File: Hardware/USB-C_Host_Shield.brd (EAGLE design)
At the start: 53.3 x 59.7 mm, 55 parts, among them J1 USB-C, J2 GPIN, J3 GPOUT, J4 Power Select, U1 ARDUINO_UNO_R3_SHIELDBASIC, U2 LM1117, U3 74HC4050, U5 MAX3421, U6 3.3V/150mA, Y1 12.0mhZ

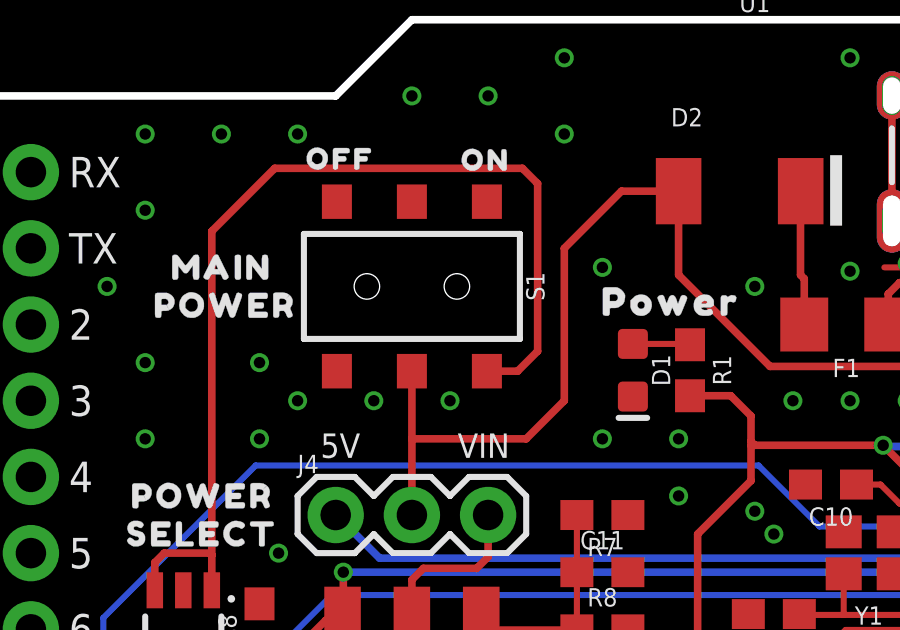
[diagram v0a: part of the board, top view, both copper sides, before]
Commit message: Added more GND vias and adjusted traces
Continued adding GNDing vias with adjusted traces for more polygon connection
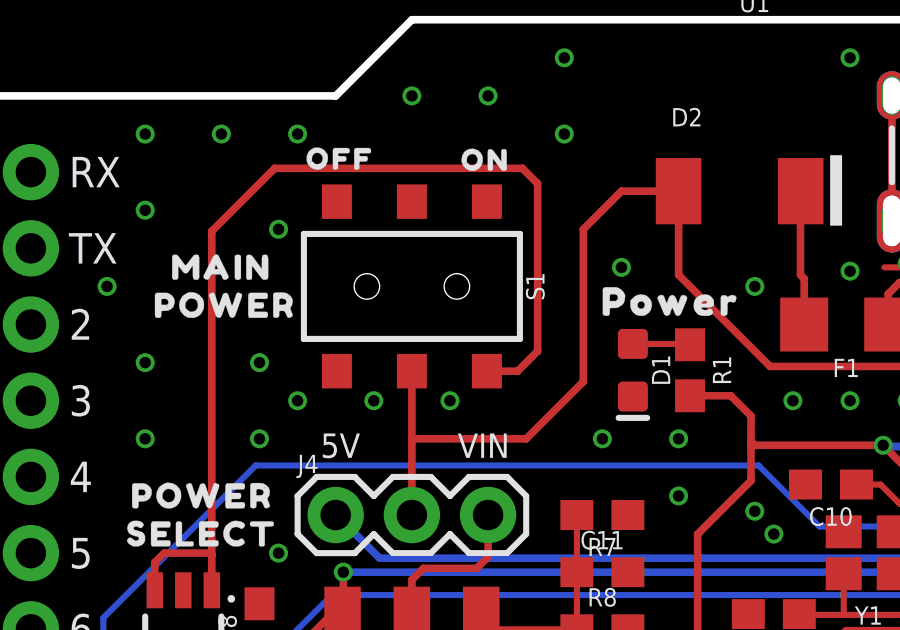
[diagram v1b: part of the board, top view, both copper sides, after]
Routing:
- net GND: vias 98 -> 99
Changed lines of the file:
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@@
 <drawing>
 <settings>
-<setting alwaysvectorfont="yes"/>
+<setting alwaysvectorfont="no"/>
 <setting verticaltext="up"/>
 </settings>
-<grid distance="50" unitdist="mil" unit="mil" style="lines" multiple="1" display="yes" altdistance="5" altunitdist="mil" altunit="mil"/>
+<grid distance="0.05" unitdist="inch" unit="inch" style="lines" multiple="1" display="yes" altdistance="0.005" altunitdist="inch" altunit="inch"/>
 <layers>
 <layer number="1" name="Top" color="4" fill="1" visible="yes" active="yes"/>
@@
 <layer number="44" name="Drills" color="7" fill="1" visible="no" active="yes"/>
 <layer number="45" name="Holes" color="7" fill="1" visible="yes" active="yes"/>
-<layer number="46" name="Milling" color="3" fill="1" visible="yes" active="yes"/>
+<layer number="46" name="Milling" color="3" fill="1" visible="no" active="yes"/>
 <layer number="47" name="Measures" color="7" fill="1" visible="no" active="yes"/>
 <layer number="48" name="Document" color="7" fill="1" visible="no" active="yes"/>
@@
 <via x="8.89" y="34.29" extent="1-16" drill="0.381"/>
 <via x="5.08" y="31.75" extent="1-16" drill="0.381"/>
-<via x="21.59" y="51.435" extent="1-16" drill="0.381"/>
+<via x="22.225" y="51.435" extent="1-16" drill="0.381"/>
 <via x="26.67" y="50.8" extent="1-16" drill="0.381"/>
 <via x="27.94" y="46.99" extent="1-16" drill="0.381"/>
@@
 <via x="34.29" y="30.48" extent="1-16" drill="0.381"/>
 <via x="44.45" y="39.37" extent="1-16" drill="0.381"/>
+<via x="10.795" y="52.705" extent="1-16" drill="0.381"/>
 </signal>
 <signal name="N$7">
@@
 <contactref element="D2" pad="A"/>
 <wire x1="24.13" y1="53.975" x2="22.225" y2="53.975" width="0.254" layer="1"/>
-<wire x1="20.32" y1="46.99" x2="19.05" y2="45.72" width="0.254" layer="1"/>
-<wire x1="22.225" y1="53.975" x2="20.32" y2="52.07" width="0.254" layer="1"/>
-<wire x1="20.32" y1="52.07" x2="20.32" y2="46.99" width="0.254" layer="1"/>
+<wire x1="20.955" y1="47.625" x2="19.05" y2="45.72" width="0.254" layer="1"/>
+<wire x1="22.225" y1="53.975" x2="20.955" y2="52.705" width="0.254" layer="1"/>
+<wire x1="20.955" y1="47.625" x2="20.955" y2="52.705" width="0.254" layer="1"/>
 <wire x1="15.24" y1="47.975" x2="15.24" y2="45.72" width="0.254" layer="1"/>
 <wire x1="15.24" y1="45.72" x2="15.24" y2="43.18" width="0.254" layer="1"/>

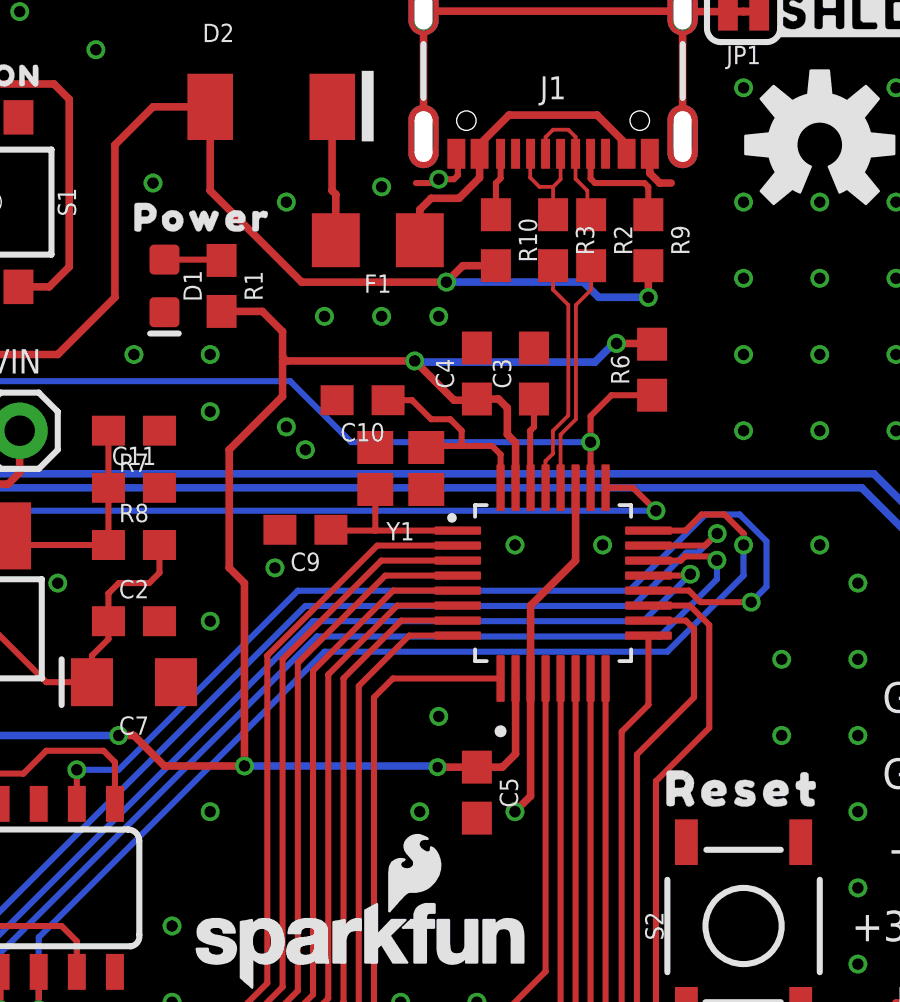
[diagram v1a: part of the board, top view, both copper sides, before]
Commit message: GND vias and connection
Adjusted for better connection and removed wire stubs
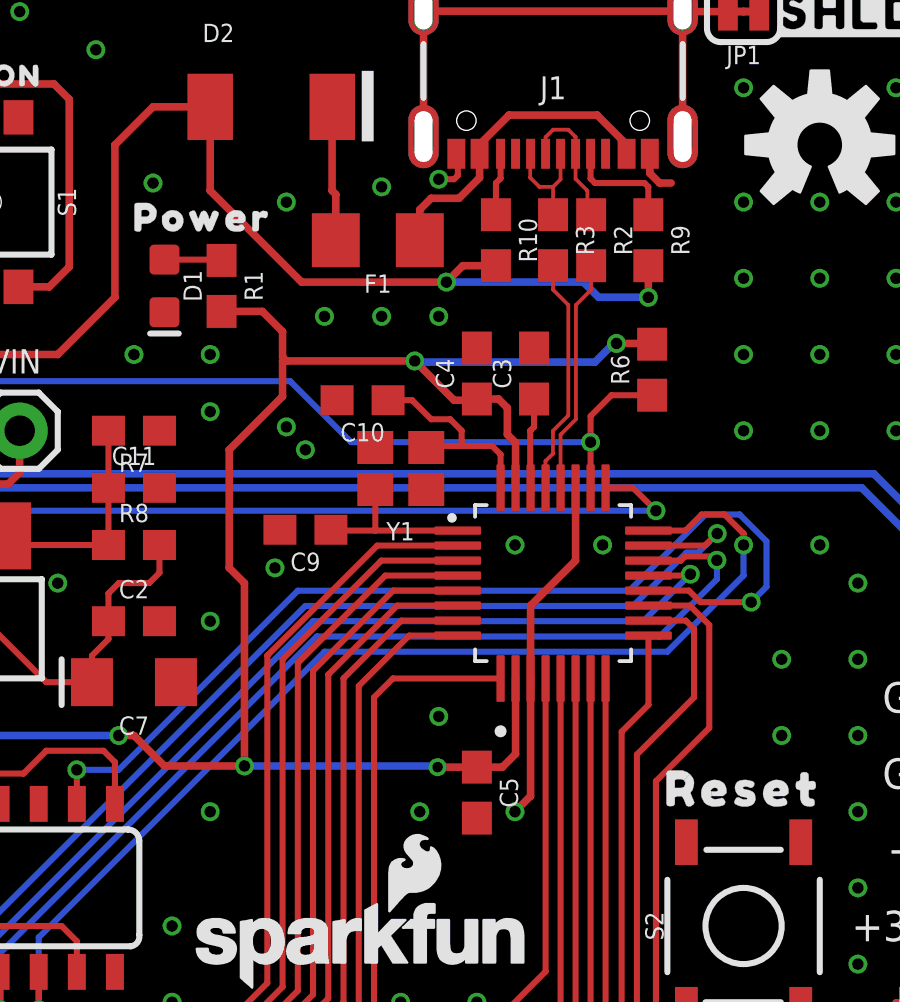
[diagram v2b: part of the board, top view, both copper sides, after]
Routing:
- net GND: track 15.7 -> 14.7 mm
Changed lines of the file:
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@@
 <vertex x="2.54" y="0"/>
 </polygon>
-<wire x1="33.02" y1="30.265" x2="33.235" y2="30.48" width="0.254" layer="1"/>
 <via x="6.35" y="20.955" extent="1-16" drill="0.381"/>
 <via x="5.08" y="1.27" extent="1-16" drill="0.381"/>
@@
 <wire x1="32.385" y1="52.36" x2="32.335" y2="52.41" width="0.2032" layer="1"/>
 <wire x1="31.75" y1="51.562" x2="31.623" y2="51.435" width="0.2032" layer="1"/>
-<wire x1="31.623" y1="51.435" x2="30.988" y2="51.435" width="0.2032" layer="1"/>
 <via x="8.89" y="34.29" extent="1-16" drill="0.381"/>
 <via x="5.08" y="31.75" extent="1-16" drill="0.381"/>
@@
 <via x="37.211" y="39.37" extent="1-16" drill="0.381"/>
 <wire x1="38.785" y1="52.41" x2="38.785" y2="51.7609" width="0.254" layer="1"/>
-<wire x1="39.1109" y1="51.435" x2="39.497" y2="51.435" width="0.254" layer="1"/>
-<wire x1="38.785" y1="51.7609" x2="39.1109" y2="51.435" width="0.254" layer="1"/>
 <via x="12.065" y="34.29" extent="1-16" drill="0.381"/>
 <via x="19.05" y="38.1" extent="1-16" drill="0.381"/>
@@
 <via x="44.45" y="39.37" extent="1-16" drill="0.381"/>
 <via x="10.795" y="52.705" extent="1-16" drill="0.381"/>
+<wire x1="39.1109" y1="51.435" x2="39.497" y2="51.435" width="0.254" layer="1"/>
+<wire x1="38.785" y1="51.7609" x2="39.1109" y2="51.435" width="0.254" layer="1"/>
 </signal>
 <signal name="N$7">

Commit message: Updates for design review
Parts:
- added LOGO1: OSHW-LOGOM, SparkFun-Aesthetics:OSHW-LOGO-M
- added U$16: (no value), output:GPOUT44
- added U$17, U$29: (no value), output:045
- added U$18, U$30: (no value), output:146
- added U$19, U$31: (no value), output:2147
- added U$20, U$32: (no value), output:32148
- added U$21, U$22: (no value), output:4332150
- added U$23, U$25: (no value), output:54332151
- added U$24, U$26: (no value), output:654332152
- added U$27, U$28: (no value), output:7654332153
- U$3: device SparkFun-Aesthetics:OSHW-LOGO-M -> output:GPIN42
- moved U$3 43.4 mm to (14.9, 21.0)
- moved R3 1.98 mm to (34.0, 48.3)
- moved R10 1.89 mm to (32.3, 48.3)
- moved C4 1.80 mm to (31.8, 43.8)
- moved D1 1.80 mm to (21.3, 46.7)
- moved FD3 1.80 mm to (45.7, 57.1)
- moved FD4 1.80 mm to (45.7, 57.1)
- moved J1 1.80 mm to (34.3, 50.8)
- moved R6 1.80 mm to (37.6, 43.9)
- moved U5 1.80 mm to (34.3, 36.8)
- moved C6 1.80 mm to (7.62, 34.3)
- moved U$13 1.80 mm to (6.99, 41.3)
- moved U$15 1.80 mm to (7.62, 50.2)
- moved C1 1.80 mm to (8.26, 31.8)
- moved C5 1.80 mm to (31.8, 29.8)
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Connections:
- net GND: no longer S1.3
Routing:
- net 3.3V: track 87.5 -> 84.5 mm
- net RESET-IN: track 33.8 -> 32.5 mm
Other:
- board text removed: "0"
- board text removed: "1"
- board text removed: "2"
- board text removed: "3"
- board text removed: "4"
- board text removed: "5"
- board text removed: "6"
- board text removed: "7"
- board text removed: "GPIN"
- board text removed: "GPOUT"

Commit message: Further changes for design review made
Working through SF Board Checklist now
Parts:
- removed U$10: (no value), SparkFun-Aesthetics:SFE_LOGO_NAME_FLAME_.1
- added LOGO2: SFE_LOGO_NAME_FLAME.1_INCH, SparkFun-Aesthetics:SFE_LOGO_NAME_FLAME_.1
- moved LOGO1 1.80 mm to (44.5, 50.8)
- moved R6 1.80 mm to (38.9, 42.7)
- moved U$11 1.80 mm to (45.5, 54.6)
- moved U$8 1.80 mm to (48.0, 46.5)
- moved U$7 1.80 mm to (12.8, 52.5)
- moved U3 1.80 mm to (16.5, 25.4)
- moved U$12 1.80 mm to (8.26, 41.3)
- moved U$4 1.80 mm to (8.89, 25.4)
- moved U6 1.80 mm to (7.62, 36.8)
- moved FRAME1 1.80 mm to (1.27, -33.0)
- moved C10 1.80 mm to (29.2, 41.7)
- moved C11 1.80 mm to (21.6, 38.7)
- moved C2 1.80 mm to (21.6, 34.3)
- moved C5 1.80 mm to (33.0, 28.6)
- moved C8 1.80 mm to (10.2, 36.8)
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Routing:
- net 3.3V: track 84.5 -> 87.5 mm
- net RESET-IN: track 32.5 -> 33.8 mm

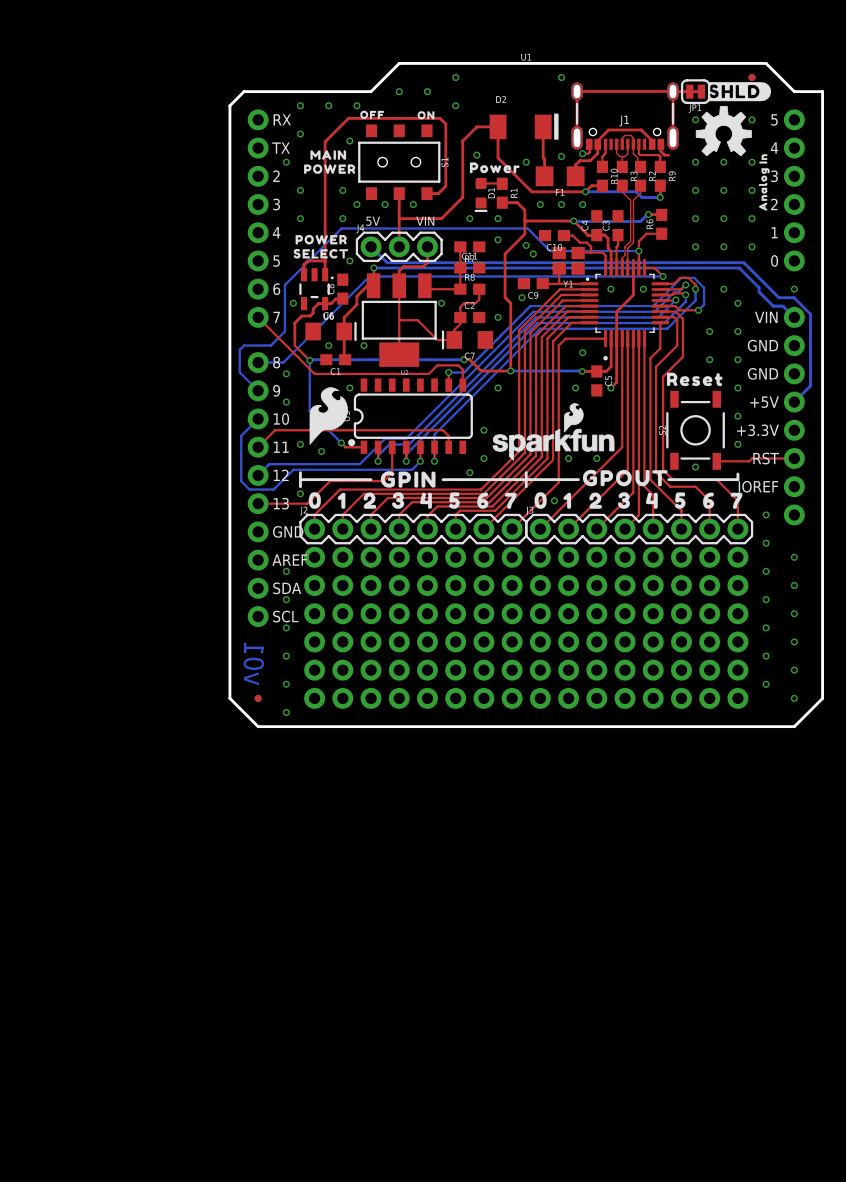
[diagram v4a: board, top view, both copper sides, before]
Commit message: Updates for design review notes
Made more updates according to design review notes. Updated prod_id for the MAX3421
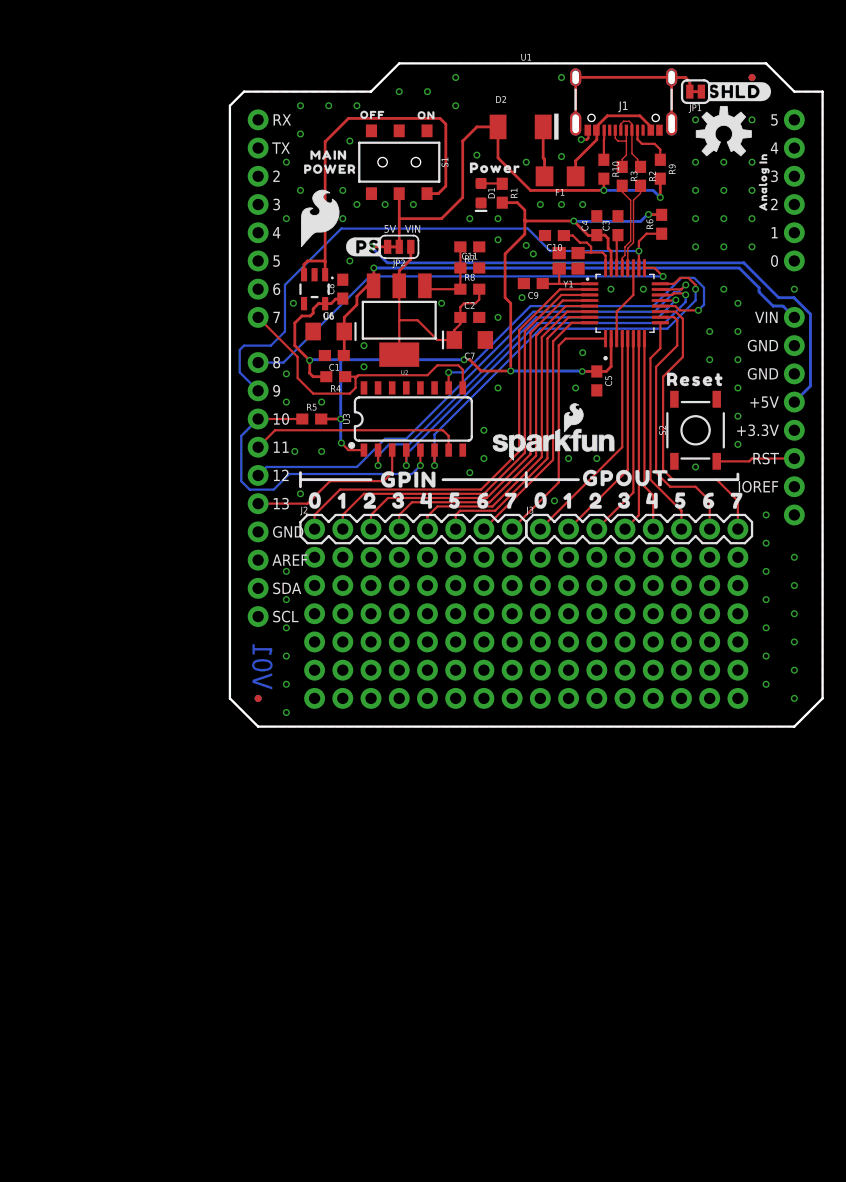
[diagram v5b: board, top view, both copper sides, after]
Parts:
- removed J4: Power Select, SparkFun-Connectors:1X03
- removed U$1: (no value), SparkFun-Aesthetics:SFE_LOGO_NAME_WEB
- removed U$12: (no value), output:POWER38
- removed U$13: (no value), output:SELECT37
- added JP2: Power Select, SparkFun-Jumpers:SMT-JUMPER_3_1-NC_TRACE_SILK
- added LOGO3: SFE_LOGO_NAME_FLAME.2_INCH, SparkFun-Aesthetics:SFE_LOGO_NAME_FLAME_.2
- added R4, R5: 2.2k, SparkFun-Resistors:0603
- added U$10: (no value), output:#PS7654332156
- moved U$4 17.8 mm to (8.13, 43.2)
- moved J1 1.28 mm to (35.4, 50.8)
- moved R10 0.65 mm to (33.7, 47.6)
- moved R9 0.63 mm to (38.7, 47.6)
- moved C1 0.40 mm to (9.40, 30.9)
- moved U3 0.25 mm to (16.5, 25.1)
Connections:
- net 3.3V: now also R4.2, R5.2
- net 5V: now also JP2.3; no longer J4.1
- net CS: now also R5.1
- net N$6: now also JP2.1; no longer J4.3
- net RESET: now also R4.1
- net VDD: now also JP2.2; no longer J4.2
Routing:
- net GND: track 14.7 -> 8.71 mm, vias 99 -> 98
- net RESET: track 22.4 -> 26.8 mm
- net CS: track 25.0 -> 28.9 mm
- net 3.3V: track 87.5 -> 91.0 mm, vias 7 -> 8
- net N$6: track 23.6 -> 21.9 mm
- net D_P: track 3.82 -> 5.29 mm
- net 5V: track 50.6 -> 52.0 mm, vias 0 -> 1
- net D_N: track 4.63 -> 5.95 mm
- net N$8: track 18.5 -> 19.7 mm
- net VBUS: track 10.6 -> 11.3 mm
- net CC2: track 2.15 -> 2.68 mm
- net PICO-IN: track 37.2 -> 37.7 mm
- net CS-IN: track 35.8 -> 36.3 mm
- net SCK-IN: track 35.8 -> 36.3 mm
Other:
- board text added: "V01"
- board text removed: "v01"
